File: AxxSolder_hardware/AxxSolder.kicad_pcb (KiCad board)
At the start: 2 copper layers, 39 x 82.5 mm, 134 parts, among them IC1 OPA2387DSGT, IC2 TPD4E1B06DRLR, IC3 TPS54302DDCR, IC4 STUSB4500QTR, IC5 LTC4440AHMS8E, IC6 MAX16171ATA_VY+T, IC7 STM32G431CBT6, J1 USB4110-GF-A, J2 691243110009, J3 61300611821, J4 TSW-102-07-T-S, J5 TSW-102-07-T-S, Q1 STL9P3LLH6, Q2 2N7002NXAKR, Q3 STL10N3LLH5, U2 PEC11J-9215F-S0015, U4 BSC014N04LS

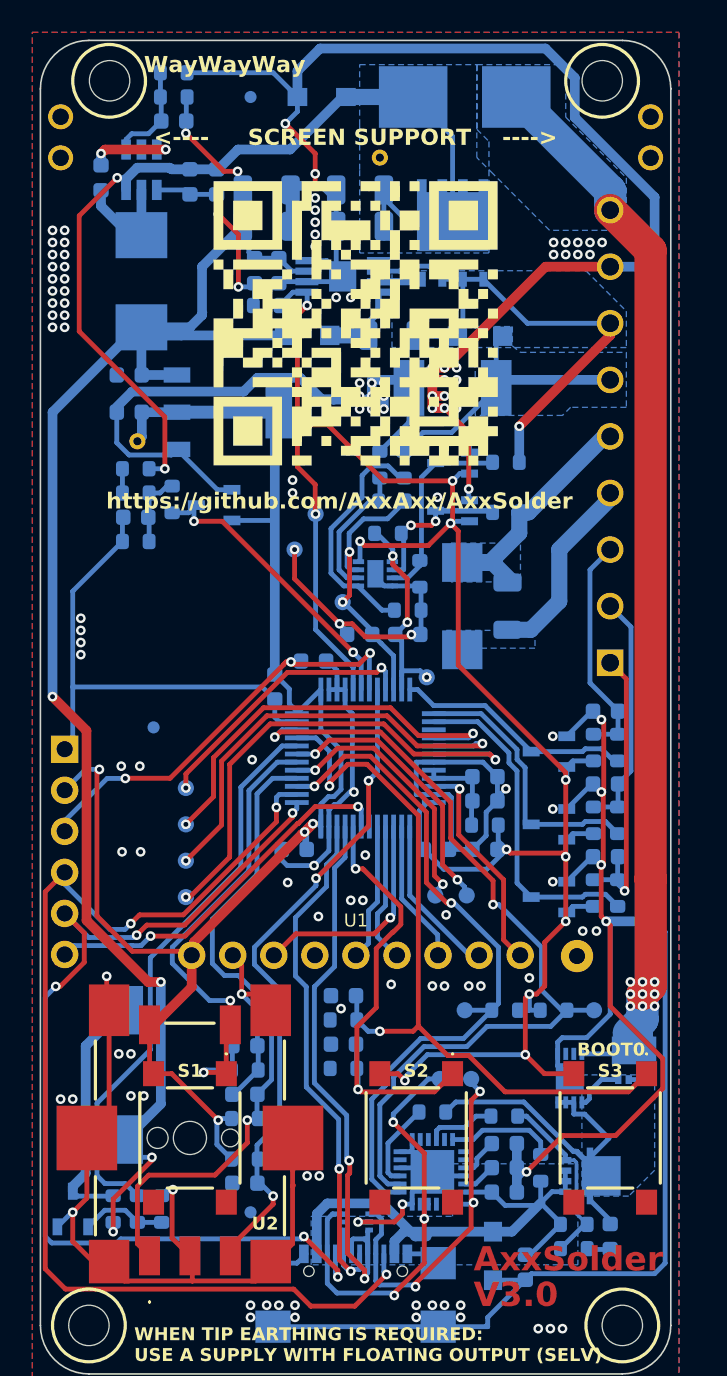
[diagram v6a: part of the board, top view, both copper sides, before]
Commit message: Updates on hardware, new DC-DC step down driver, new LDO, new ESD protection for USB, new Capacitor selection on input
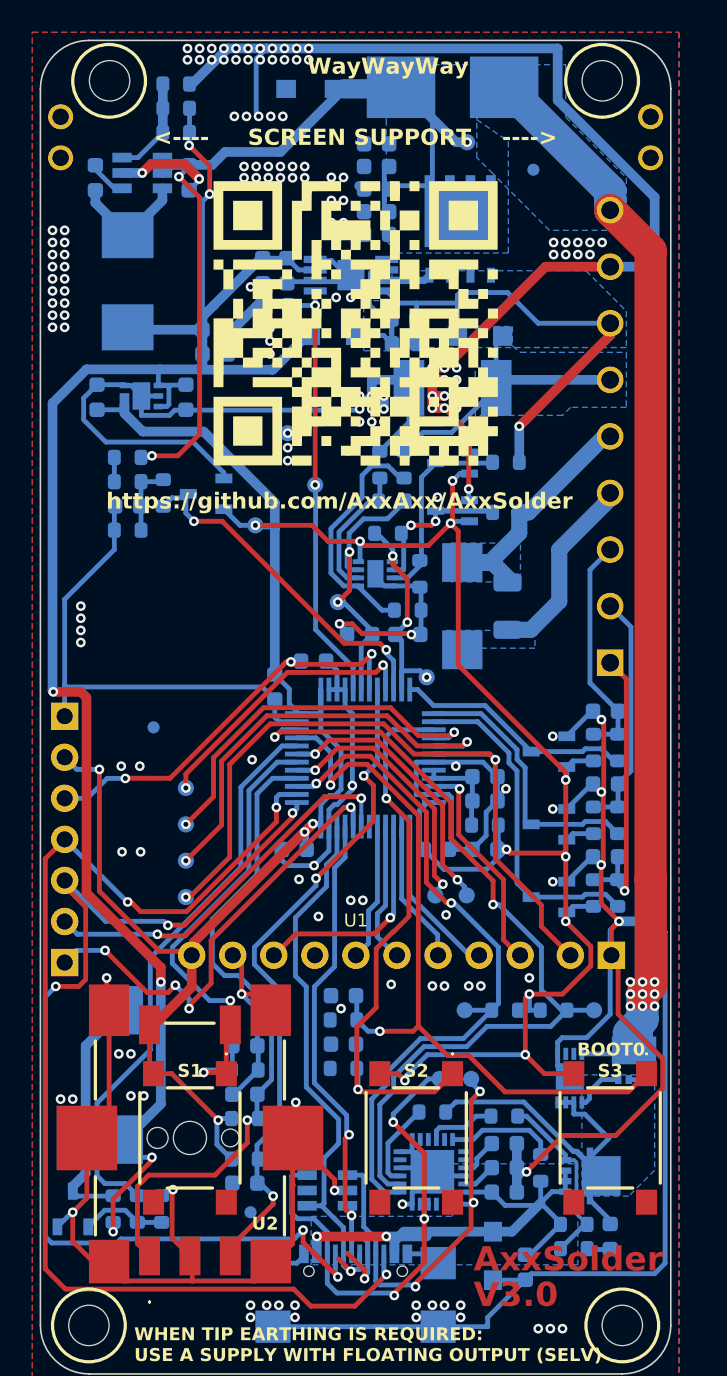
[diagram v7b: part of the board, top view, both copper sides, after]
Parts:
- removed C39: 22u/35V, Capacitor_SMD:C_1206_3216Metric
- removed the C5 at (170.2, 76.2)
- removed the C9 at (175.0, 79.0)
- removed the IC2 at (180.5, 140.6)
- removed PS1: LD1117AS33TR, footprints:SOT230P700X190-4N
- removed the R6 at (169.2, 71.0)
- removed the TP6 at (194.2, 124.2)
- removed the TP7 at (182.0, 74.8)
- added C30: 10u, Capacitor_SMD:C_0603_1608Metric, B.Cu at (183.5, 84.8)
- added C31: 10u, Capacitor_SMD:C_0603_1608Metric, B.Cu at (183.5, 86.3)
- added C34: 10u, Capacitor_SMD:C_0603_1608Metric, B.Cu at (181.8, 79.5)
- added C36: 10u, Capacitor_SMD:C_0603_1608Metric, B.Cu at (181.8, 76.7)
- added C37: 10u, Capacitor_SMD:C_0603_1608Metric, B.Cu at (181.8, 75.3)
- added IC1: TLV76733DRVR, footprints:SON65P200X200X80-7N, B.Cu at (167.2, 89.5)
- added IC5: TPD4E1U06DBVR, footprints:SOT95P280X145-6N, B.Cu at (178.8, 138.7)
- added J3: TSW-102-07-T-S, Connector_PinHeader_2.54mm:PinHeader_1x02_P2.54mm_Vertical, B.Cu at (196.3, 124.1)
- added R7: 360k, Resistor_SMD:R_0603_1608Metric, B.Cu at (169.4, 71.7)
- added R8: 360k, Resistor_SMD:R_0603_1608Metric, B.Cu at (169.4, 73.2)
- added TP13: DIAG_TP, Connector_PinSocket_2.54mm:PinSocket_1x01_P2.54mm_Vertical, B.Cu at (162.5, 124.5)
- added TP9: 7.5V_TP, TestPoint:TestPoint_Pad_D1.0mm, B.Cu at (187.4, 73.8)
- C1: value 100n -> 10u
- C35, C8: value 22u -> 10u; footprint Capacitor_SMD:C_1206_3216Metric -> Capacitor_SMD:C_0603_1608Metric
- C38: value 22u/35V -> 10u; footprint Capacitor_SMD:C_1206_3216Metric -> Capacitor_SMD:C_0603_1608Metric
- C7: value 75p -> 10u
- IC3: value TPS54302DDCR -> LMR54406DBVR; footprint footprints:SOT95P280X110-6N -> footprints:SOT95P280X145-6N
- J5: renamed from J4; moved to B.Cu
- J6: renamed from J5; moved to B.Cu
- L1: value SRP7028CC -> SRP7028CC-150M
- TP12: renamed from TP14; value TC_TP -> GND_TP
- TP3: renamed from TP2; footprint TestPoint:TestPoint_THTPad_D1.0mm_Drill0.5mm -> TestPoint:TestPoint_Pad_D1.0mm
- moved FID3 18.1 mm to (191.5, 75.5)
- moved C7 14.6 mm to (171.8, 86.9), turned to 180 degrees
- moved C8 9.22 mm to (171.8, 85.4)
- moved TP3 8.96 mm to (174.3, 97.5)
- moved C35 7.71 mm to (181.8, 78.1), turned to 0 degrees
- moved TP12 7.21 mm to (176.3, 91.8)
- moved C1 3.76 mm to (170.0, 89.6), turned to -90 degrees
- moved C38 3.03 mm to (181.8, 73.9), turned to 0 degrees
- moved C2 2.20 mm to (164.5, 89.6), turned to 90 degrees
- moved J4 2.04 mm to (162.5, 109.3)
- moved TP17 1.80 mm to (178.0, 95.0)
- moved C5 1.72 mm to (170.2, 76.0)
- moved D9 1.60 mm to (179.1, 85.8)
- moved F1 0.96 mm to (186.5, 70.4)
- moved D4 0.86 mm to (177.7, 70.5)
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- renumbered C19 to C10, C16 to C11, C15 to C12, C12 to C13, C20 to C15, C21 to C16, C22 to C17, C24 to C18, C25 to C19, C3 to C20, C26 to C21, C27 to C22, C28 to C23, C29 to C24, C30 to C25, C31 to C26, C32 to C27, C33 to C28, C34 to C29, C4 to C3, C36 to C32, C37 to C33, C10 to C4, C6 to C5, C11 to C6, C13 to C9, D13 to D10, FID3 to FID1, FID1 to FID3, IC1 to IC2, IC7 to IC4, IC4 to IC6, IC6 to IC7, IC5 to IC8, J3 to J4, Q3 to Q2, Q2 to Q3, R9 to R10, R10 to R11, R11 to R12, R12 to R13, R13 to R14, R14 to R15, R40 to R16, R15 to R17, R16 to R18, R17 to R19, R18 to R20, R41 to R21, R19 to R22, R20 to R23, R21 to R24, R22 to R25, R23 to R26, R24 to R27, R25 to R28, R26 to R29, R27 to R30, R28 to R31, R29 to R32, R30 to R33, R31 to R34, R32 to R35, R33 to R36, R34 to R37, R35 to R38, R39 to R42, R7 to R6, R8 to R9, TP18 to TP1, TP4 to TP10, TP5 to TP11, TP13 to TP14, TP11 to TP15, TP12 to TP16, TP8 to TP17, TP19 to TP2, TP9 to TP4, TP1 to TP5, TP10 to TP6, TP16 to TP7, TP17 to TP8, U4 to U3
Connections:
- C1 pad 1: GND -> +7.5V
- C1 pad 2: +6V -> GND
- C3 pad 1: Net-(IC3-BOOT) -> Net-(IC3-CB)
- C32 pad 1: +6V -> +7.5V
- C33 pad 1: +6V -> +7.5V
- C35 pad 1: /RED -> GND
- C35 pad 2: Net-(IC5-TS) -> VDD
- C38 pad 1: VDD -> GND
- C38 pad 2: GND -> VDD
- C7 pad 1: Net-(IC3-FB) -> GND
- C7 pad 2: +6V -> +7.5V
- C8 pad 2: +6V -> +7.5V
- D9 pad 1: Net-(IC5-TS) -> /BOOST
- D9 pad 2: +6V -> +7.5V
- IC3 pad 1: GND -> Net-(IC3-CB)
- IC3 pad 2: Net-(IC3-SW) -> GND
- IC3 pad 3: VDD -> Net-(IC3-FB)
- IC3 pad 4: Net-(IC3-FB) -> VDD
- IC3 pad 5: unconnected-(IC3-EN-Pad5) -> VDD
- IC3 pad 6: Net-(IC3-BOOT) -> Net-(IC3-SW)
- IC4 pad 10: /CURRENT -> /VBUS_IN
- IC4 pad 15: unconnected-(IC7-PA7-Pad15) -> /SW2
- IC4 pad 32: /SW2 -> /USART_RX
- IC4 pad 6: /VBUS_IN -> /CURRENT
- IC8 pad 3: +6V -> +7.5V
- IC8 pad 6: /RED -> /BOOST
- IC8 pad 8: Net-(IC5-TS) -> /RED
- L1 pad 2: +6V -> +7.5V
- LS1 pad 2: +6V -> +7.5V
- R23 pad 1: +6V -> +7.5V
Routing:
- net +7.5V: track 0.00 -> 112.2 mm, vias 0 -> 6
- net +6V: track 110.7 -> 0.00 mm, vias 6 -> 0
- net /USART_RX: track 0.00 -> 29.0 mm, vias 0 -> 4
- net GND: track 481.5 -> 467.2 mm, vias 132 -> 170
- net /USR4: track 31.8 -> 45.8 mm
- net VDD: track 59.4 -> 69.0 mm, vias 2 -> 3
- net /BOOST: track 0.00 -> 8.23 mm
- net /SW2: track 28.6 -> 36.6 mm
- net Net-(IC5-TS): track 5.42 -> 0.00 mm
- net Net-(IC3-BOOT): track 5.38 -> 0.00 mm, vias 2 -> 0
- net /CC2: track 27.8 -> 31.9 mm
- net +3.3V: track 200.4 -> 196.7 mm
- net /SWDIO: track 61.7 -> 65.1 mm
- net /VBUS_IN: track 18.5 -> 21.5 mm
- net /CC1: track 24.2 -> 27.1 mm
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- added copper zone on B.Cu, net /BOOST
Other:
- board text added: "2024-02"
- board text added: "RX"
- board text added: "VIN"
- board text removed: "2024-01"
- board text removed: "G431CBT6"
- board text removed: "V_IN"

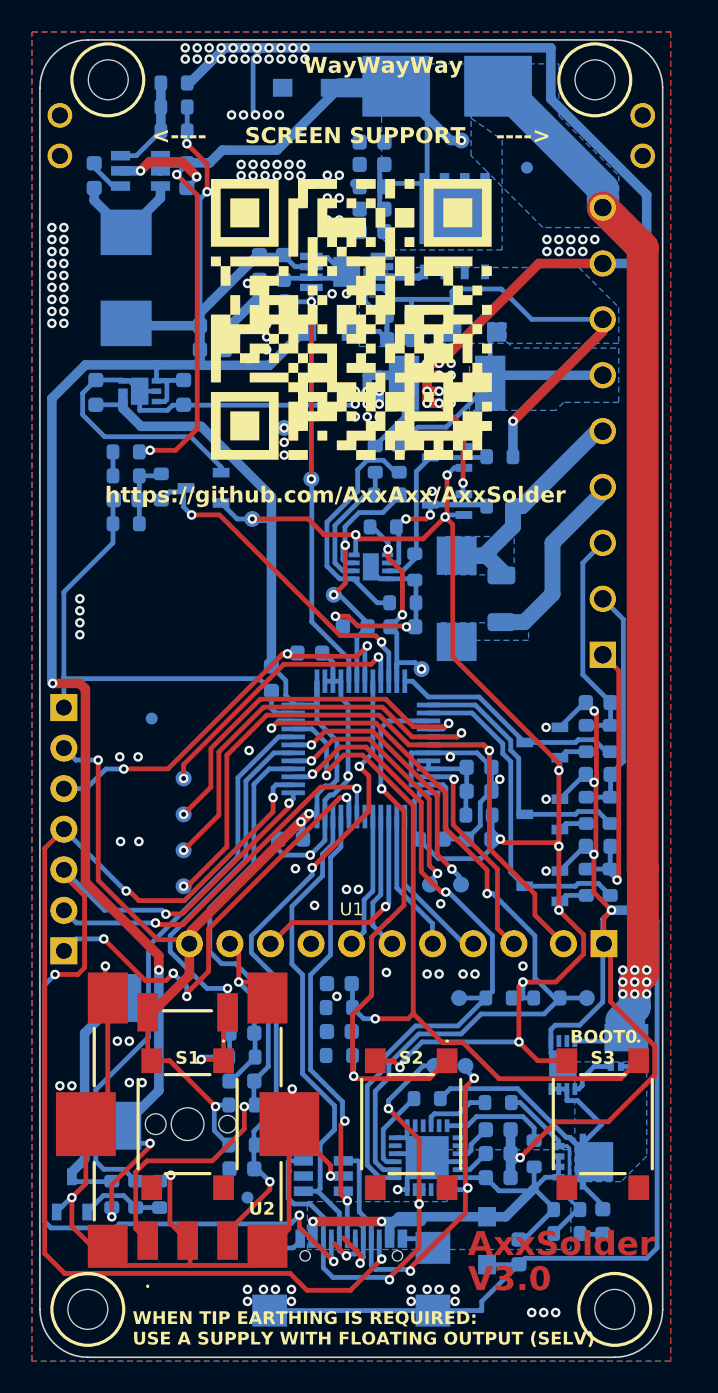
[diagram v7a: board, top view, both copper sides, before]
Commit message: update design with new electrolytic capacitor
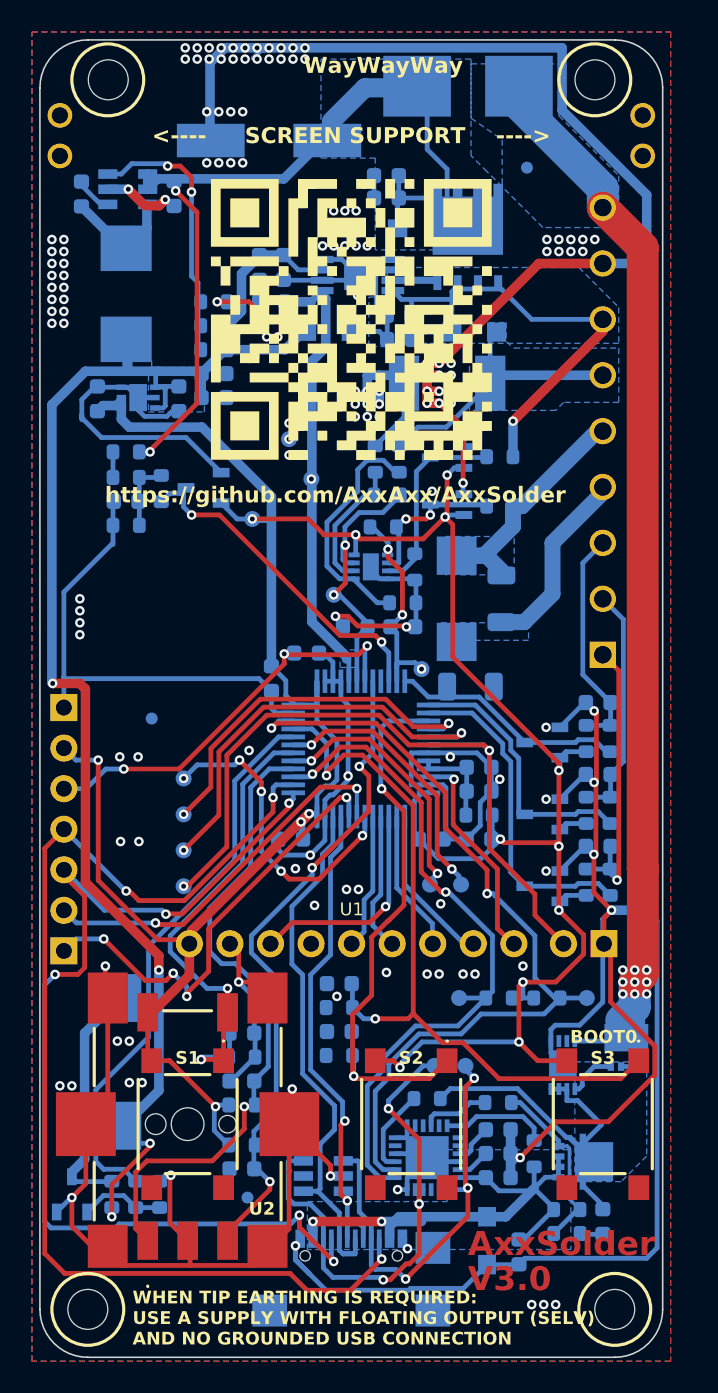
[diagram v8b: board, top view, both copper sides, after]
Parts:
- removed C36, C38: 10u, Capacitor_SMD:C_0603_1608Metric
- removed TP9: 7.5V_TP, TestPoint:TestPoint_Pad_D1.0mm
- added R43: 1M, Resistor_SMD:R_1206_3216Metric, B.Cu at (188.0, 108.0)
- C37: value 10u -> 220u; footprint Capacitor_SMD:C_0603_1608Metric -> footprints:CAPAE830X1050N
- moved R11 13.9 mm to (171.9, 83.9)
- moved R7 13.9 mm to (171.9, 85.4)
- moved R8 13.9 mm to (171.9, 86.9)
- moved D4 9.75 mm to (181.9, 79.3)
- moved C37 6.62 mm to (175.3, 73.8), turned to 180 degrees
- moved C7 3.00 mm to (171.9, 89.9)
- moved C8 3.00 mm to (171.9, 88.4)
- moved C34 2.28 mm to (182.7, 77.4)
- moved C35 2.28 mm to (182.7, 76.0)
- moved C3 1.40 mm to (163.6, 77.2)
- moved IC3 1.40 mm to (166.5, 76.8)
- moved C5 1.38 mm to (169.4, 77.1)
- moved F1 1.31 mm to (187.8, 70.4)
- moved U3 1.06 mm to (187.8, 76.8)
- moved L1 1.00 mm to (166.4, 83.4)
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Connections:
- C37 pad 1: GND -> VDD
- C37 pad 2: VDD -> GND
- IC4 pad 30: unconnected-(IC4-PA8-Pad30) -> /USR1
- IC4 pad 9: /USR1 -> unconnected-(IC4-PA1-Pad9)
- J1 pad S1: GND -> unconnected-(J1-SHIELD-PadS1)
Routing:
- net GND: track 467.2 -> 449.0 mm, vias 170 -> 151
- net +7.5V: track 112.2 -> 95.8 mm, vias 6 -> 4
- net Net-(IC3-FB): track 5.97 -> 16.9 mm, vias 0 -> 2
- net VDD: track 69.0 -> 59.9 mm, vias 3 -> 2
- net /USB_D-: track 34.6 -> 30.9 mm, vias 3 -> 2
- net /USR1: track 17.4 -> 19.7 mm, vias 2 -> 5
- net /Heater: track 27.3 -> 28.4 mm, vias 2 -> 1
- net /RED: track 34.1 -> 33.3 mm
- net /CC1: track 27.1 -> 27.6 mm
- net /USB_D+: track 34.4 -> 34.0 mm, vias 1 -> 0
- added copper zone on B.Cu, net +7.5V
- added copper zone on B.Cu, net /Heater
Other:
- board text added: "WHEN TIP EARTHING IS REQUIRED: USE A SUPPLY WITH FLOATING OUTPUT (SELV) AND NO GROUNDED USB CONNECTION"
- board text removed: "WHEN TIP EARTHING IS REQUIRED: USE A SUPPLY WITH FLOATING OUTPUT (SELV)"
